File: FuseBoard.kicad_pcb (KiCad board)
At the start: 2 copper layers, 130 x 100 mm, 22 parts, among them J1 Conn_01x02_Socket, J10 Conn_01x02_Socket, J2 Conn_01x02_Socket, J3 Conn_01x02_Socket, J4 Conn_01x02_Socket, J5 Conn_01x02_Socket, J6 Conn_01x02_Socket, J7 Conn_01x02_Socket, J8 Conn_01x02_Socket, J9 Conn_01x02_Socket

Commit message: changes to pcb
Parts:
- added J11: Conn_01x02_Socket, Connector_AMASS:AMASS_XT30PW-M_1x02_P2.50mm_Horizontal, F.Cu at (115.0, 70.0)
- moved J9 114.6 mm to (115.0, 90.0), turned to 90 degrees
- moved F1 18.5 mm to (159.3, 123.5)
- moved F2 18.5 mm to (169.3, 123.5)
- moved F3 18.5 mm to (179.3, 123.5)
- moved F4 18.5 mm to (196.8, 123.5)
- moved F5 18.5 mm to (149.3, 123.5)
- moved F6 18.5 mm to (206.8, 123.5)
- moved F7 18.5 mm to (216.8, 123.5)
- moved F8 18.5 mm to (226.8, 123.5)
- moved J1 18.5 mm to (151.0, 136.7)
- moved J10 18.5 mm to (133.5, 136.7)
- moved J2 18.5 mm to (161.0, 136.7)
- moved J3 18.5 mm to (171.0, 136.7)
- moved J4 18.5 mm to (181.0, 136.9)
- moved J5 18.5 mm to (198.5, 136.9)
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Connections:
- J1 pad 1: Net-(J1-Pin_1) -> GND
- J2 pad 1: Net-(J1-Pin_1) -> GND
- J3 pad 1: Net-(J1-Pin_1) -> GND
- J4 pad 1: Net-(J1-Pin_1) -> GND
- J5 pad 1: Net-(J5-Pin_1) -> GND
- J6 pad 1: Net-(J5-Pin_1) -> GND
- J7 pad 1: Net-(J5-Pin_1) -> GND
- J8 pad 1: Net-(J5-Pin_1) -> GND
- J9 pad 1: Net-(J9-Pin_1) -> GND
- U2 pad 1: (no net) -> GND
- U3 pad 1: (no net) -> GND
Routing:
- net GND: track 0.00 -> 206.3 mm
- net Net-(J9-Pin_2): track 0.00 -> 124.7 mm
- net Net-(J10-Pin_1): track 0.29 -> 58.1 mm
- net Net-(J11-Pin_2): track 0.00 -> 42.1 mm
- net Net-(J1-Pin_1): track 30.1 -> 0.00 mm
- net Net-(J5-Pin_1): track 30.0 -> 0.00 mm
- net Net-(U3-OUT+): track 3.40 -> 19.2 mm
- net Net-(U1-OUT+): track 33.4 -> 41.7 mm
- net Net-(U2-OUT+): track 33.4 -> 41.7 mm
- added copper zone on B.Cu, net GND
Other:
- board size 130 x 100 mm -> 135 x 100 mm

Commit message: updated pcb
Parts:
- moved J11 5.67 mm to (120.7, 70.0)
- moved J9 5.67 mm to (120.7, 90.0)
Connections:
- net Net-(U1-OUT+) renamed +5V
- net Net-(U2-OUT+) renamed +12V
- U2 pad 1: GND -> (no net)
- U3 pad 1: GND -> (no net)
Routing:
- net Net-(J9-Pin_2): track 124.7 -> 119.0 mm
- net Net-(J11-Pin_2): track 42.1 -> 36.4 mm
- net GND: track 206.3 -> 210.7 mm
- net Net-(J10-Pin_1): track 58.1 -> 57.5 mm
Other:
- board size 135 x 100 mm -> 127.5 x 100 mm

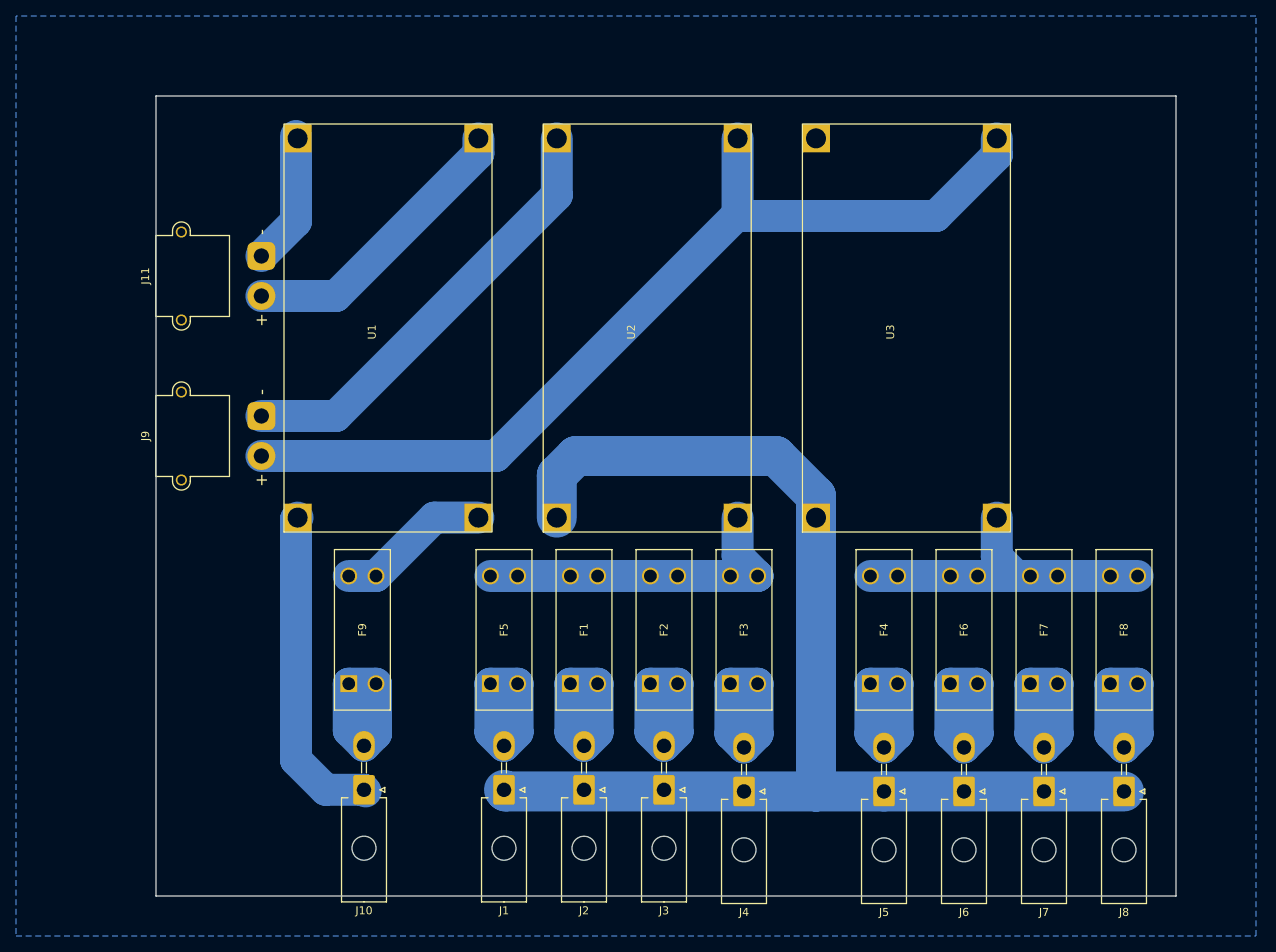
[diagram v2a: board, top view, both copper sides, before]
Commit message: separated GNDs
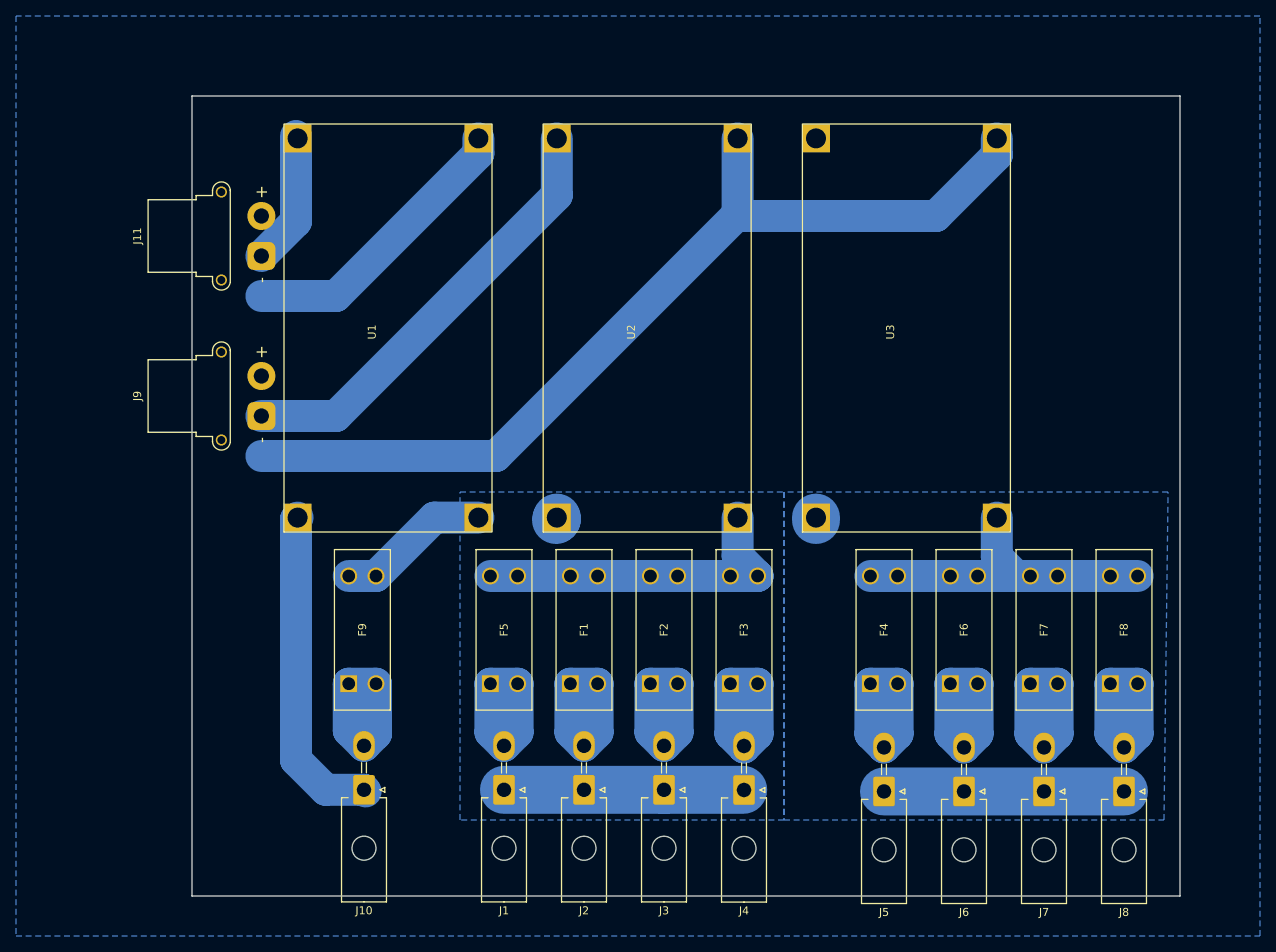
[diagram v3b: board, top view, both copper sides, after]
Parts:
- J11, J9: footprint Connector_AMASS:AMASS_XT30PW-M_1x02_P2.50mm_Horizontal -> Connector_AMASS:AMASS_XT30PW-F_1x02_P2.50mm_Horizontal
- moved J4 0.18 mm to (181.0, 136.8)
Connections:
- J1 pad 1: GND -> GND1
- J2 pad 1: GND -> GND1
- J3 pad 1: GND -> GND1
- J4 pad 1: GND -> GND1
- J5 pad 1: GND -> GND2
- J6 pad 1: GND -> GND2
- J7 pad 1: GND -> GND2
- J8 pad 1: GND -> GND2
- U2 pad 1: (no net) -> GND1
- U3 pad 1: (no net) -> GND2
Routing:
- net GND: track 210.7 -> 55.5 mm
- net GND2: track 0.00 -> 30.3 mm
- net GND1: track 0.00 -> 30.2 mm
- added copper zone on B.Cu, net GND1
- added copper zone on B.Cu, net GND2
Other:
- board size 127.5 x 100 mm -> 123.5 x 100 mm
